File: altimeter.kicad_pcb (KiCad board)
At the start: 2 copper layers, 18 x 86 mm, 52 parts, among them IC1 MS5611-01BA03, IC2 ADP1607, IC3 STM32F411CxUx, J1 BATT, P1 SWD_TC, Q1 NFET, U1 MICROSD, X1 M3 Hole, X2 M3 Hole, Y1 26MHz

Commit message: finished board
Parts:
- moved C17 14.6 mm to (106.8, 98.8), turned to 0 degrees
- moved R10 7.34 mm to (102.6, 91.2), turned to 180 degrees
- moved TP6 6.69 mm to (102.7, 92.8)
- moved TP2 4.39 mm to (100.0, 78.2)
- moved TP3 4.30 mm to (98.7, 81.4)
- moved R1 4.19 mm to (93.7, 126.6)
- moved R5 3.72 mm to (103.9, 126.6)
- moved R7 3.53 mm to (102.3, 126.6)
- moved R8 3.45 mm to (96.9, 126.6)
- moved TP7 3.30 mm to (96.7, 81.4)
- moved C4 3.28 mm to (95.3, 126.6)
- moved R3 3.28 mm to (92.1, 126.6)
- moved TP5 2.08 mm to (100.7, 85.4)
- moved C9 2.00 mm to (95.6, 83.2), turned to 180 degrees
- moved R12 1.20 mm to (102.3, 85.4)
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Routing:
- net 3v3: track 0.00 -> 191.8 mm, vias 0 -> 11
- net GND: track 0.00 -> 57.3 mm, vias 0 -> 28
- net /BEEPER: track 0.00 -> 51.9 mm, vias 0 -> 2
- net /SDIO_D0: track 0.00 -> 39.7 mm, vias 0 -> 2
- net /SDIO_D3: track 0.00 -> 39.5 mm, vias 0 -> 3
- net /SDIO_D1: track 0.00 -> 37.1 mm
- net /SDIO_D2: track 0.00 -> 36.5 mm
- net /SDIO_CMD: track 0.00 -> 27.1 mm, vias 0 -> 3
- net /SDIO_CK: track 0.00 -> 23.4 mm, vias 0 -> 2
- net /~RST: track 0.00 -> 21.2 mm, vias 0 -> 2
- net /STAT_HBT: track 0.00 -> 19.6 mm, vias 0 -> 2
- net VBATT: track 0.00 -> 19.3 mm
- net /SWDIO: track 0.00 -> 17.1 mm, vias 0 -> 2
- net /I2C1_SDA: track 0.00 -> 15.6 mm
- net /SWCLK: track 0.00 -> 14.2 mm, vias 0 -> 2
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- added copper zone on B.Cu, net GND
- added copper zone on F.Cu, net GND
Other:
- net class Default: clearance 0.2 -> 0.15
- rule trace_clearance: 0.2 -> 0.15
- rule trace_min: 0.2 -> 0.1524
- rule via_min_size: 0.4 -> 0.6
- board text added: "+"
- board text added: "CUSF Altimeter"
- board text added: "mc955"

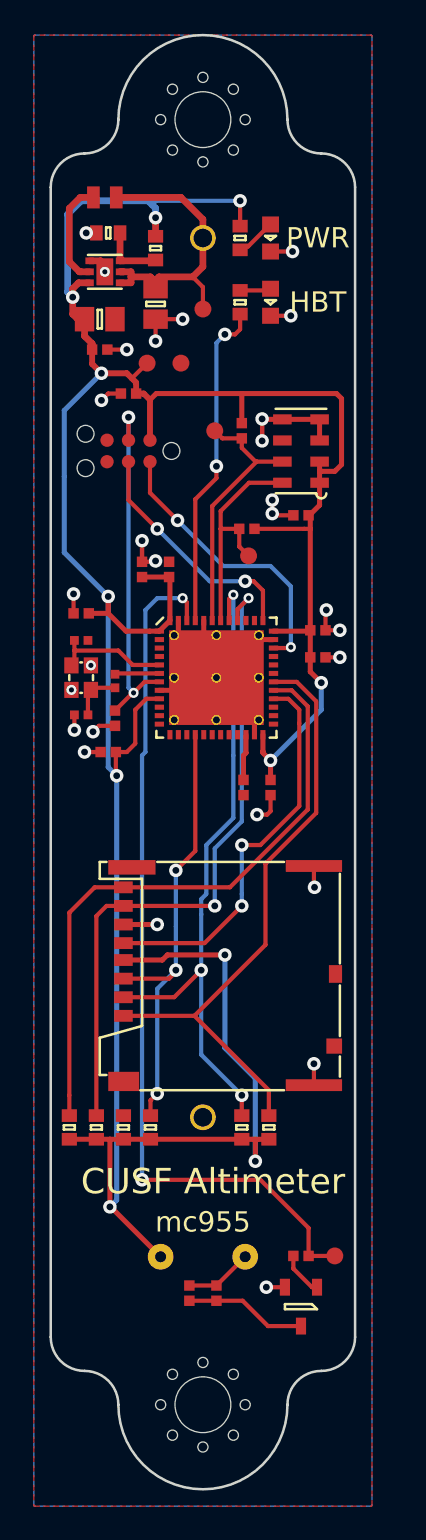
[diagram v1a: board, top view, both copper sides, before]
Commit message: added panel and updated bom
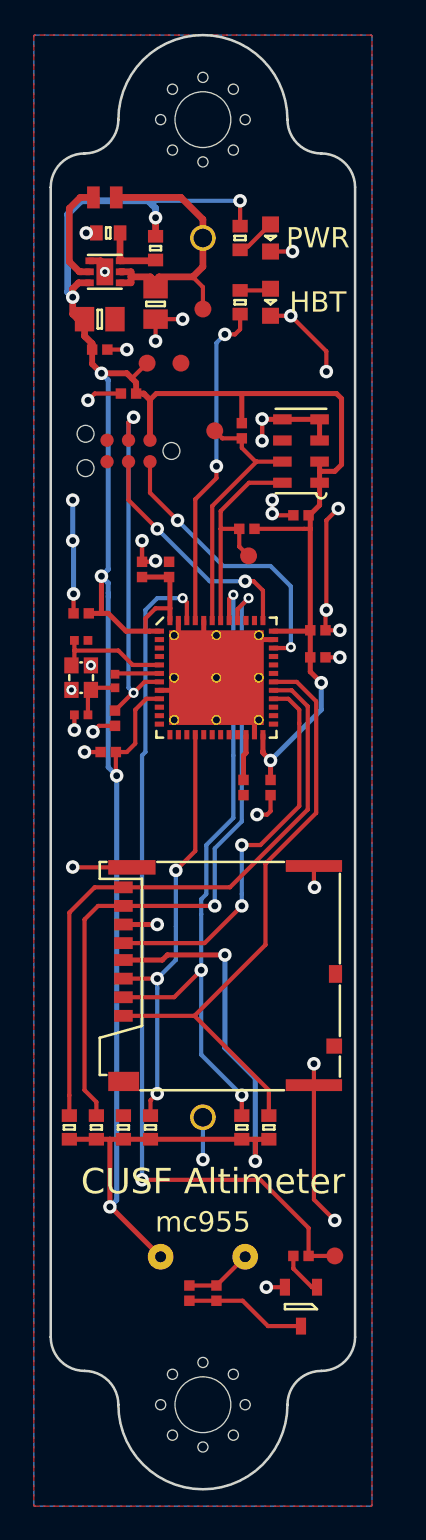
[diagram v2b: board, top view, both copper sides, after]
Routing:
- net GND: track 57.3 -> 88.6 mm, vias 28 -> 35
- net /SDIO_CMD: track 27.1 -> 25.6 mm
- net 3v3: track 191.8 -> 193.1 mm
- net /SDIO_D0: track 39.7 -> 40.5 mm
